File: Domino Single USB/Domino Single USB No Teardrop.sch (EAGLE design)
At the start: 13 parts, among them J1 MH10-1, J2 USB_AF-006, J3 MH10-1

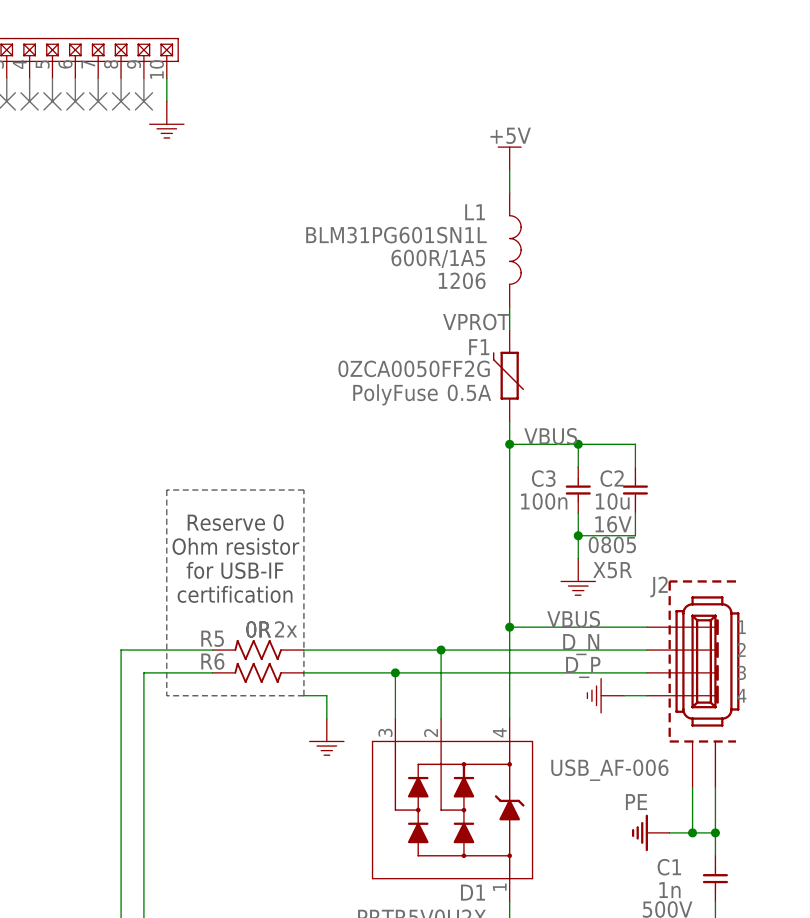
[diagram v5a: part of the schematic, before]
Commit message: Domino Single USB Rev. C: removed the resetable fuse that causes too much drop for high-current USB devices
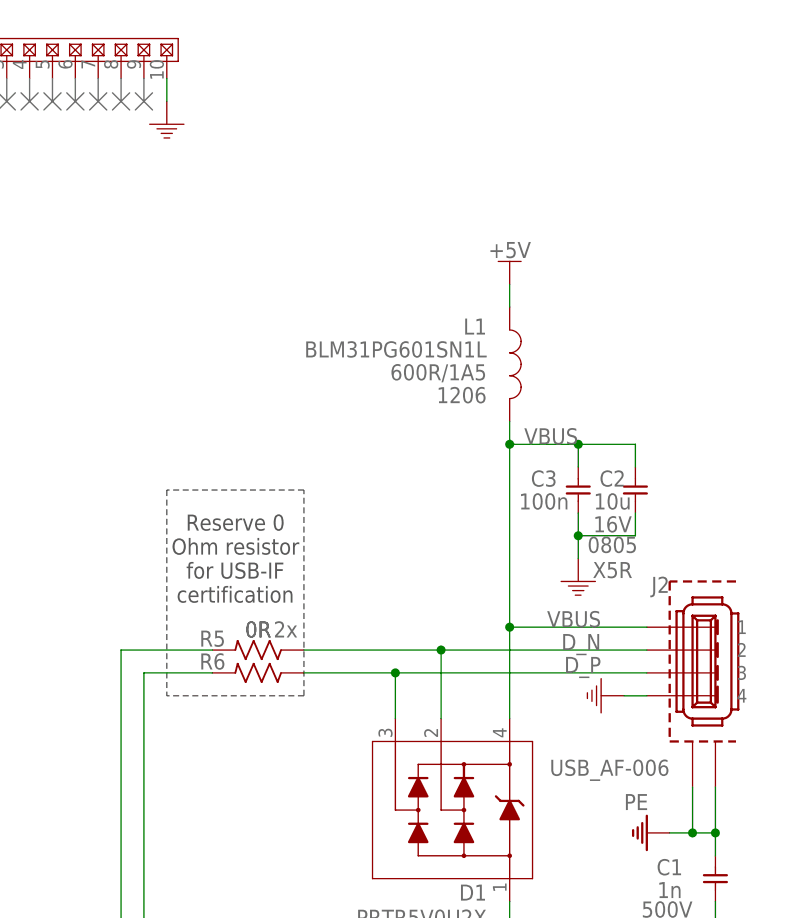
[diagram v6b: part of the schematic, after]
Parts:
- removed F1: 0ZCA0050FF2G, Domino:0ZCA0050FF2G
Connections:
- removed net VPROT: F1.1, L1.2
- net VBUS: now also L1.2; no longer F1.2
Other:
- note removed: "PolyFuse"
- moved on the sheet: L1
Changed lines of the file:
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@@
 <attribute name="VOLT" value="16V"/>
 </part>
-<part name="F1" library="Domino" deviceset="0ZCA" device="" technology="0050FF2G" value="0ZCA0050FF2G">
-<attribute name="PARTNO" value="0ZCG0110FF2C"/>
-</part>
-<part name="SUPPLY1" library="Domino" deviceset="GND" device=""/>
 <part name="J2" library="Domino" deviceset="USB_AF-006" device="">
 <attribute name="PARTNO" value="USB_AF-006"/>
@@
 <text x="379.222" y="5.334" size="1.778" layer="94">&gt;REV</text>
 <text x="374.142" y="5.334" size="1.778" layer="94">Rev.</text>
-<text x="210.566" y="167.386" size="1.778" layer="96" rot="MR0">PolyFuse</text>
 <text x="193.548" y="141.986" size="1.778" layer="95" rot="MR0" align="center">2x</text>
 <text x="187.96" y="149.86" size="1.778" layer="97" rot="MR0" align="center">Reserve 0
@@
 </instance>
 <instance part="SUPPLY38" gate="GND" x="226.06" y="149.86" rot="MR0"/>
-<instance part="L1" gate="G$1" x="218.44" y="185.42" smashed="yes" rot="R270">
-<attribute name="SIZE" x="215.9" y="181.61" size="1.778" layer="96" rot="R180"/>
-<attribute name="OPT" x="215.9" y="184.15" size="1.778" layer="96" rot="R180"/>
-<attribute name="PARTNO" x="218.44" y="185.42" size="1.778" layer="96" rot="MR180" display="off"/>
-<attribute name="NAME" x="215.9" y="189.23" size="1.778" layer="95" rot="R180"/>
-<attribute name="VALUE" x="215.9" y="186.69" size="1.778" layer="96" rot="R180"/>
+<instance part="L1" gate="G$1" x="218.44" y="172.72" smashed="yes" rot="R270">
+<attribute name="SIZE" x="215.9" y="168.91" size="1.778" layer="96" rot="R180"/>
+<attribute name="OPT" x="215.9" y="171.45" size="1.778" layer="96" rot="R180"/>
+<attribute name="PARTNO" x="218.44" y="172.72" size="1.778" layer="96" rot="MR180" display="off"/>
+<attribute name="NAME" x="215.9" y="176.53" size="1.778" layer="95" rot="R180"/>
+<attribute name="VALUE" x="215.9" y="173.99" size="1.778" layer="96" rot="R180"/>
 </instance>
 <instance part="C2" gate="G$1" x="232.41" y="157.48" smashed="yes" rot="MR270">
@@
 <attribute name="VALUE" x="229.87" y="156.21" size="1.778" layer="96" rot="MR180" align="center"/>
 </instance>
-<instance part="F1" gate="G$1" x="218.44" y="170.18" smashed="yes" rot="MR180">
-<attribute name="OPT" x="220.98" y="154.94" size="1.778" layer="96" rot="MR90"/>
-<attribute name="RATE" x="216.408" y="167.386" size="1.778" layer="96" rot="MR0"/>
-<attribute name="PARTNO" x="218.44" y="170.18" size="1.778" layer="96" rot="MR90" display="off"/>
-<attribute name="NAME" x="216.3826" y="172.466" size="1.778" layer="95" rot="MR0"/>
-<attribute name="VALUE" x="216.408" y="170.053" size="1.778" layer="96" rot="MR0"/>
-</instance>
-<instance part="SUPPLY1" gate="GND" x="198.12" y="132.08"/>
 <instance part="J2" gate="G$1" x="238.76" y="139.7" smashed="yes" rot="MR0">
 <attribute name="NAME" x="236.22" y="146.05" size="1.778" layer="95" rot="MR0"/>
@@
 <attribute name="PARTNO" x="167.64" y="205.74" size="1.778" layer="96" rot="MR270" display="off"/>
 </instance>
-<instance part="U$9" gate="G$1" x="218.44" y="193.04" rot="MR0"/>
+<instance part="U$9" gate="G$1" x="218.44" y="180.34" rot="MR0"/>
 <instance part="J1" gate="G$1" x="167.64" y="73.66" smashed="yes" rot="R90">
 <attribute name="VALUE" x="150.495" y="73.66" size="1.778" layer="96" rot="R180" align="center"/>
@@
 </segment>
 <segment>
-<pinref part="SUPPLY1" gate="GND" pin="GND"/>
-<wire x1="195.58" y1="134.62" x2="198.12" y2="134.62" width="0.1524" layer="91"/>
-<wire x1="198.12" y1="134.62" x2="198.12" y2="132.08" width="0.1524" layer="91"/>
-</segment>
-<segment>
 <pinref part="SUPPLY65" gate="GND" pin="GND"/>
 <wire x1="180.34" y1="78.74" x2="180.34" y2="76.2" width="0.1524" layer="91"/>
@@
 <wire x1="232.41" y1="162.56" x2="232.41" y2="160.02" width="0.1524" layer="91"/>
 <pinref part="C3" gate="G$1" pin="1"/>
-<pinref part="F1" gate="G$1" pin="2"/>
 <label x="226.06" y="162.56" size="1.778" layer="95" rot="MR0"/>
 <wire x1="226.06" y1="162.56" x2="226.06" y2="160.02" width="0.1524" layer="91"/>
@@
 <wire x1="226.06" y1="162.56" x2="218.44" y2="162.56" width="0.1524" layer="91"/>
 <junction x="226.06" y="162.56"/>
-<wire x1="218.44" y1="162.56" x2="218.44" y2="165.1" width="0.1524" layer="91"/>
 <junction x="218.44" y="162.56"/>
 <pinref part="J2" gate="G$1" pin="1"/>
+<pinref part="L1" gate="G$1" pin="2"/>
+<wire x1="218.44" y1="162.56" x2="218.44" y2="165.1" width="0.1524" layer="91"/>
 </segment>
 </net>
@@
 </segment>
 </net>
-<net name="VPROT" class="0">
-<segment>
-<pinref part="L1" gate="G$1" pin="2"/>
-<pinref part="F1" gate="G$1" pin="1"/>
-<wire x1="218.44" y1="177.8" x2="218.44" y2="175.26" width="0.1524" layer="91"/>
-<label x="218.44" y="175.26" size="1.778" layer="95" rot="MR0"/>
-</segment>
-</net>
 <net name="+5V" class="0">
 <segment>
@@
 <pinref part="L1" gate="G$1" pin="1"/>
 <pinref part="U$9" gate="G$1" pin="+5V"/>
-<wire x1="218.44" y1="190.5" x2="218.44" y2="193.04" width="0.1524" layer="91"/>
-</segment>
-</net>
+<wire x1="218.44" y1="177.8" x2="218.44" y2="180.34" width="0.1524" layer="91"/>
+</segment>
+</net>

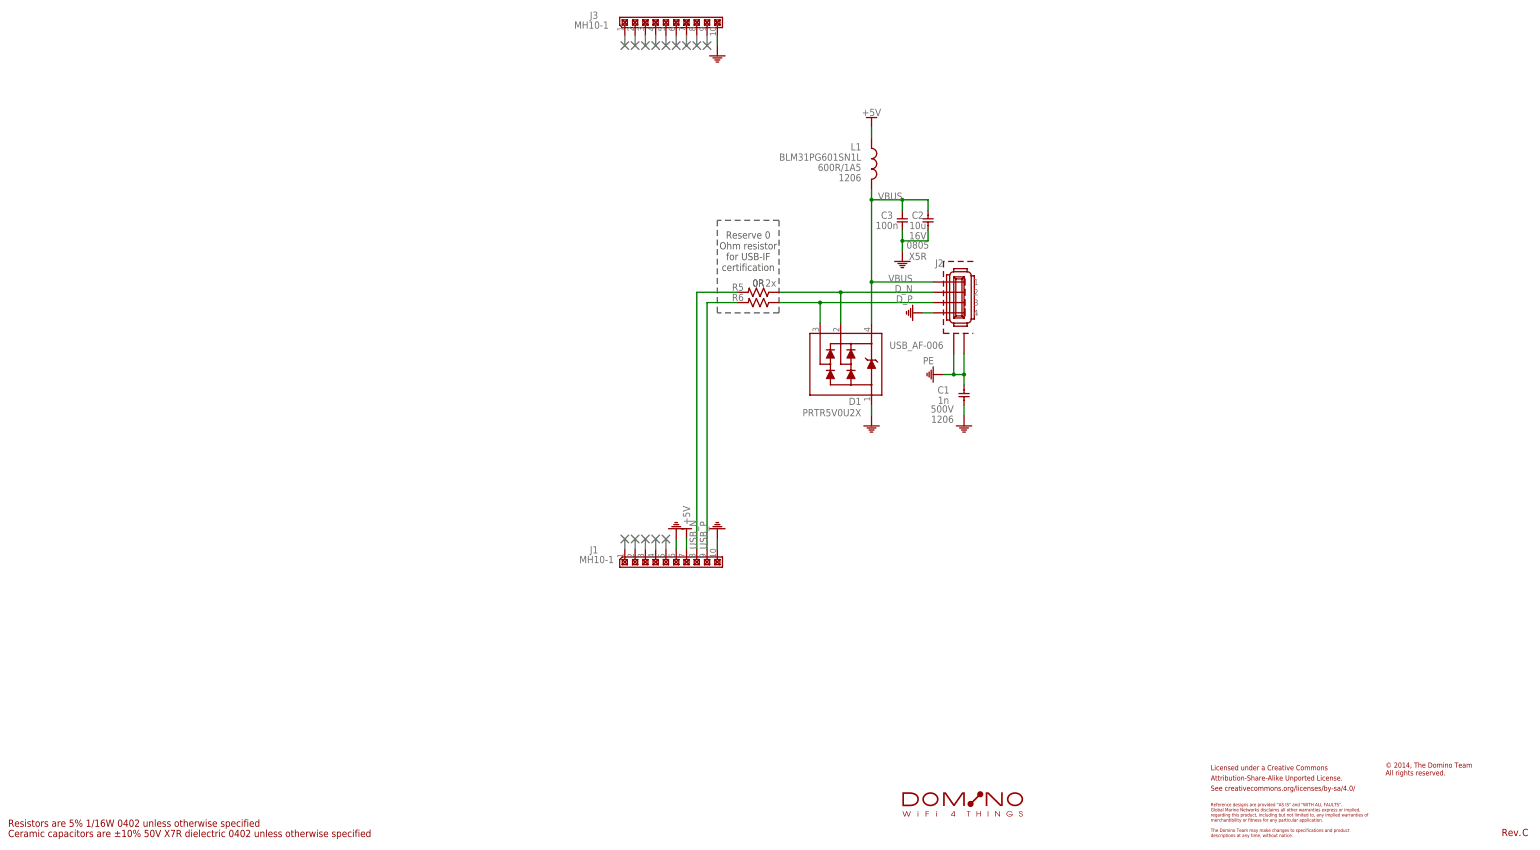
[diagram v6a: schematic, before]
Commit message: Added USB power switch to Sinfle USB tile
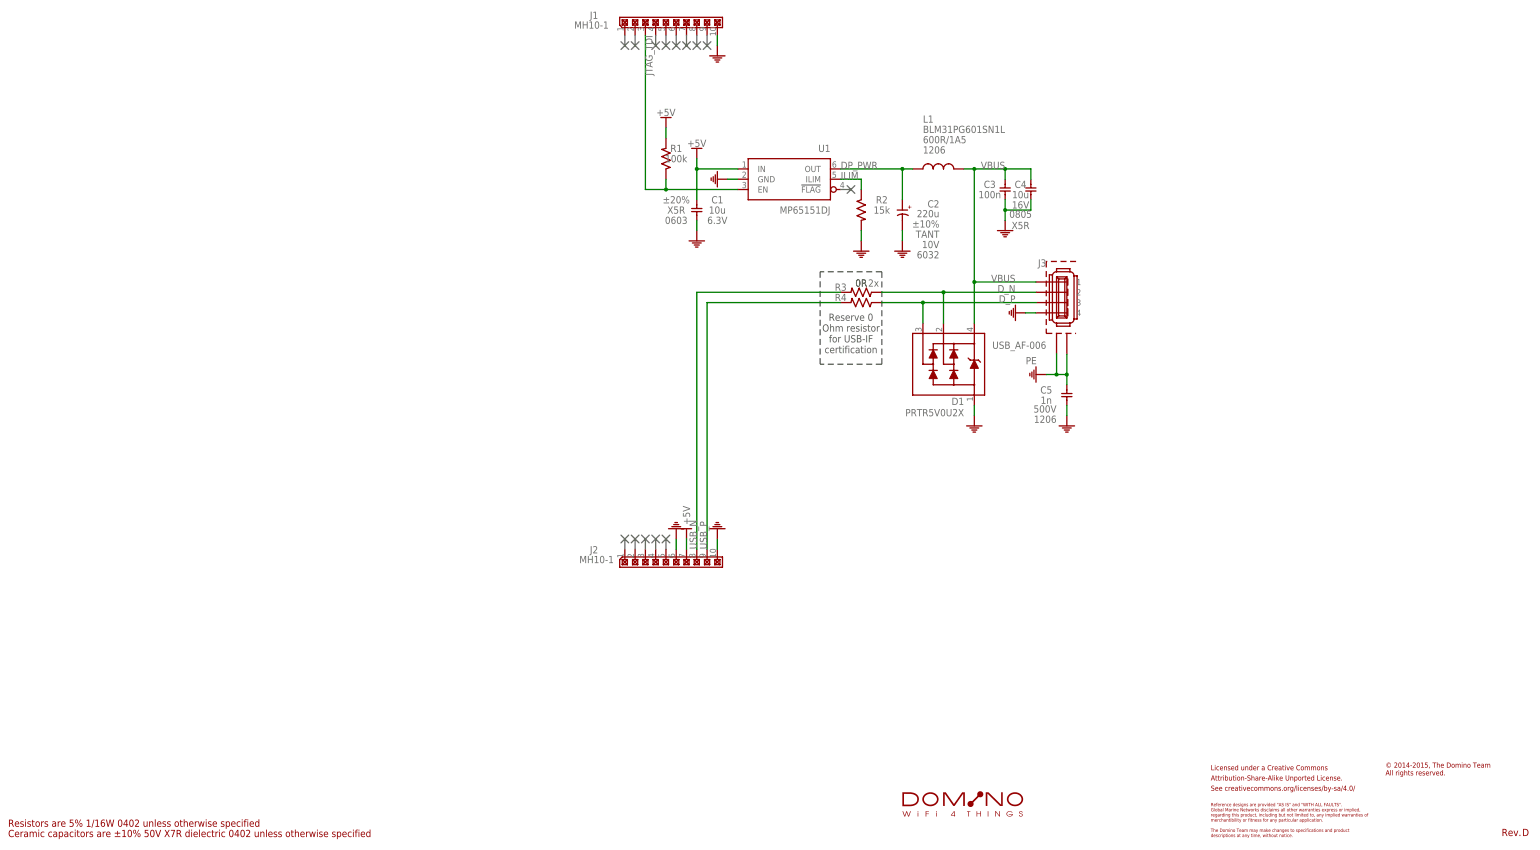
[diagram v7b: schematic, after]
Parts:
- removed R5, R6: 0R, Domino:RES_0402
- added C4: 10u, Domino:CAP_0805
- added C5: 1n, Domino:CAP_1206
- added R1: 100k, Domino:RES_0402
- added R2: 15k, Domino:RES_0402
- added R3, R4: 0R, Domino:RES_0402
- added U1: MP65151DJ, Domino:MP65151DJ
- C1: value 1n -> 10u; device Domino:CAP_1206 -> Domino:CAP_0603; PARTNO C1206_1n_X7R_10%_CER_500V -> C0603_10u_X5R_20%_CER_6V3; TC X7R -> X5R; TOL ±10% -> ±20%; VOLT 500V -> 6.3V
- C2: value 10u -> 220u; device Domino:CAP_0805 -> Domino:CPOL_C/6032-25; PARTNO C0805_10u_X5R_10%_CER_16V -> CPOLC-6032_220u_20%_TANT_10V; TC X5R -> (none); TYPE CER -> (none); VOLT 16V -> 10V
- J2: value USB_AF-006 -> MH10-1; device Domino:USB_AF-006 -> Domino:MH10-1; PARTNO USB_AF-006 -> MH10-1-0.1
- J3: value MH10-1 -> USB_AF-006; device Domino:MH10-1 -> Domino:USB_AF-006; PARTNO MH10-1-0.1 -> USB_AF-006
- renumbered U$7 to S1
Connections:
- new net DP_PWR: C2.+, L1.1, U1.OUT
- new net ILIM: R2.1, U1.ILIM
- new net JTAG_TDI: J1.3, R1.1, U1.EN
- net +5V: now also C1.1, J2.7, R1.2, U1.IN; no longer J1.7, L1.1
- net D_N: now also J3.2, R3.1; no longer J2.2, R5.1
- net D_P: now also J3.3, R4.1; no longer J2.3, R6.1
- net GND: now also C2.-, C4.2, C5.2, J2.10, J2.6, J3.4, R2.2, U1.GND; no longer C2.2, J1.6, J2.4, J3.10
- net PE: now also C5.1, J3.G@1, J3.G@2; no longer C1.1, J2.G@1, J2.G@2
- net USB_N: now also J2.8, R3.2; no longer J1.8, R5.2
- net USB_P: now also J2.9, R4.2; no longer J1.9, R6.2
- net VBUS: now also C4.1, J3.1; no longer C2.1, J2.1
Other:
- note added: "© 2014-2015, The Domino Team All rights reserved."
- note removed: "© 2014, The Domino Team All rights reserved."
- moved on the sheet: C1, C3, D1, J1, L1

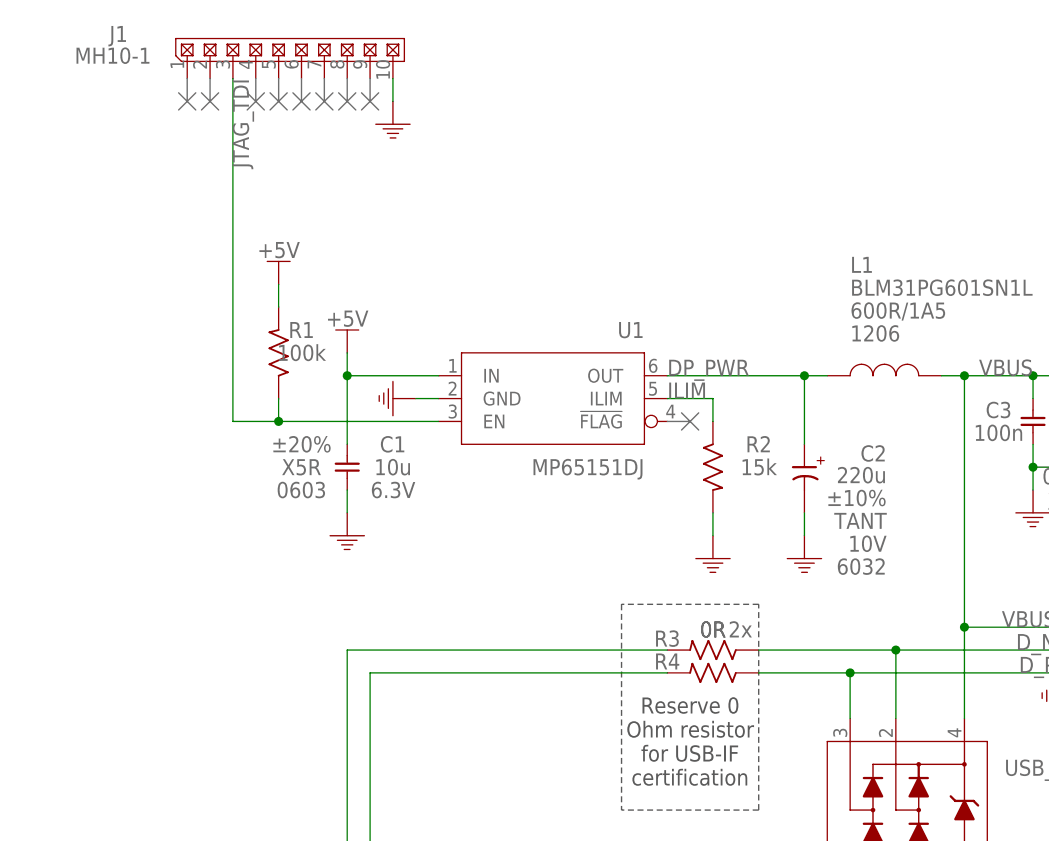
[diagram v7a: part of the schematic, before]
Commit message: Domino Single USB tile Rev. D: added resistors en power siwtch feedback and enable, changed output capacitor to smaller one
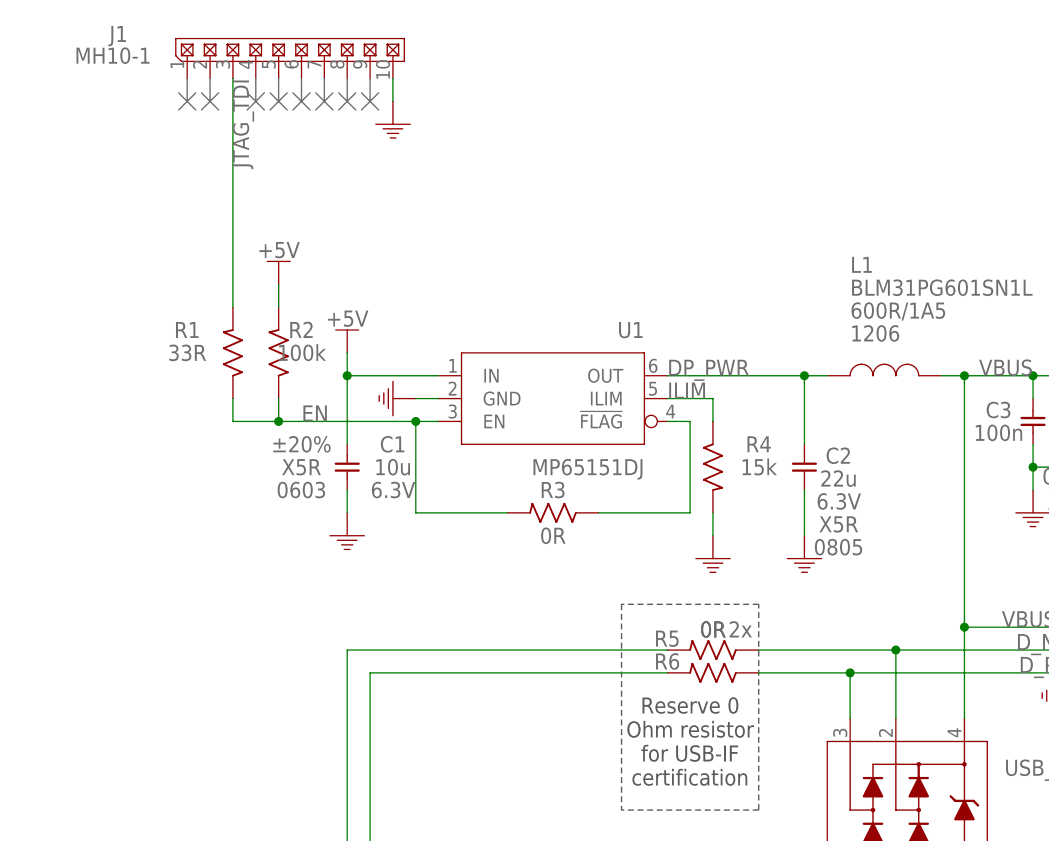
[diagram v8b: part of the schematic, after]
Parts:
- added R5, R6: 0R, Domino:RES_0402
- C2: value 220u -> 22u; device Domino:CPOL_C/6032-25 -> Domino:CAP_0805; PARTNO CPOLC-6032_220u_20%_TANT_10V -> C0805_22u_X5R_20%_CER_6V3; TC (none) -> X5R; TOL ±10% -> ±20%; TYPE (none) -> CER; VOLT 10V -> 6.3V
- R1: value 100k -> 33R; PARTNO R0402_100k_5%_62.5mW -> R0402_33R_5%_62.5mW
- R2: value 15k -> 100k; PARTNO R0402_15k_5%_62.5mW -> R0402_100k_5%_62.5mW
- R4: value 0R -> 15k; PARTNO R0402_0R_5%_62.5mW -> R0402_15k_5%_62.5mW
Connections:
- new net EN: R1.1, R2.1, R3.2, U1.EN
- new net N$1: R3.1, U1.!FLAG
- net +5V: now also R2.2; no longer R1.2
- net DP_PWR: now also C2.1; no longer C2.+
- net D_N: now also R5.1; no longer R3.1
- net D_P: now also R6.1; no longer R4.1
- net GND: now also C2.2, R4.2; no longer C2.-, R2.2
- net ILIM: now also R4.1; no longer R2.1
- net JTAG_TDI: now also R1.2; no longer R1.1, U1.EN
- net USB_N: now also R5.2; no longer R3.2
- net USB_P: now also R6.2; no longer R4.2
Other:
- moved on the sheet: R1, R2, R3, R4
